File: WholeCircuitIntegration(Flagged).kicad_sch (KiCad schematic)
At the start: 18 parts, among them J1 Conn_02x20_Odd_Even, J2 Conn_01x03_Socket, J3 Conn_01x03_Socket, J4 Conn_01x03_Socket, J5 Conn_01x03_Socket, J6 TBP03R2-350-03BE, J7 TBP03R2-350-03BE, J8 TBP03R2-350-03BE, J9 TBP03R2-350-03BE, U1 ADS1115IDGS, U2 BNO055, U3 74LV14

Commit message: Whole Circuit Integration
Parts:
- removed C1: 120, Capacitor_SMD:CP_Elec_4x3, symbol Device:C
- removed C2, C4: 100 n, Capacitor_SMD:CP_Elec_4x3, symbol Device:C
- removed C3: 6.8 n, Capacitor_SMD:CP_Elec_4x3, symbol Device:C
- removed J1: Conn_02x20_Odd_Even, symbol Connector_Generic:Conn_02x20_Odd_Even
- removed J2, J3, J4, J5: Conn_01x03_Socket, symbol Connector:Conn_01x03_Socket
- removed J6, J7, J8, J9: TBP03R2-350-03BE, TBP03R2_350_03BE:CUI_TBP03R2-350-03BE, symbol TBP03R2-350-03BE:TBP03R2-350-03BE
- removed Optional1, Pull-Up1: 10k, Resistor_SMD:R_0603_1608Metric_Pad0.98x0.95mm_HandSolder, symbol Device:R
- removed U1: ADS1115IDGS, Package_SO:TSSOP-10_3x3mm_P0.5mm, symbol Analog_ADC:ADS1115IDGS
- removed U2: BNO055, Package_LGA:LGA-28_5.2x3.8mm_P0.5mm, symbol Sensor_Motion:BNO055
- removed U3: 74LV14, Package_DIP:DIP-12_W7.62mm, symbol 74xx:74LV14
- added J6: Conn_02x20_Odd_Even, symbol Connector_Generic:Conn_02x20_Odd_Even
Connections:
- net 3.3V: now also J6.1 (Pin_1), J6.17 (Pin_17)
- net 5,0_VDC: now also J6.2 (Pin_2)
- net 5V: now also J6.4 (Pin_4)
- net ADC ALERT (GPIO 04): now also J6.7 (Pin_7)
- net COM 3 (GPIO 19): now also J6.35 (Pin_35)
- net GND: now also J6.14 (Pin_14), J6.20 (Pin_20), J6.25 (Pin_25), J6.30 (Pin_30), J6.34 (Pin_34), J6.39 (Pin_39), J6.6 (Pin_6), J6.9 (Pin_9)
- net I2C_1_SCL: now also J6.28 (Pin_28)
- net I2C_1_SDA: now also J6.27 (Pin_27)
- net I2C_2_SCL: now also J6.5 (Pin_5)
- net I2C_2_SDA: now also J6.3 (Pin_3)
- net I2S_4_SCLK: now also J6.12 (Pin_12)
- net IMU nBOOT (GPIO 13): now also J6.33 (Pin_33)
- net IMU nRESET (GPIO 05): now also J6.29 (Pin_29)
- net LCD_TE: now also J6.15 (Pin_15)
- net SPI_1_CS0: now also J6.24 (Pin_24)
- net SPI_1_CS1: now also J6.26 (Pin_26)
- net SPI_1_MISO: now also J6.21 (Pin_21)
- net SPI_1_MOSI: now also J6.19 (Pin_19)
- net SPI_1_SCK: now also J6.23 (Pin_23)
- net SPI_2_CS0: now also J6.18 (Pin_18)
- net SPI_2_CS1: now also J6.16 (Pin_16)
- net SPI_2_MISO: now also J6.22 (Pin_22)
- net SPI_2_MOSI: now also J6.37 (Pin_37)
- net SPI_2_SCK: now also J6.13 (Pin_13)
- net ST 1 (GPIO 12): now also J6.32 (Pin_32)
- net ST 2 (GPIO 16): now also J6.36 (Pin_36), J6.38 (Pin_38)
- net ST 4 (GPIO 21): now also J6.40 (Pin_40)
- net UART_2_RTS: now also J6.11 (Pin_11)
- net UART_2_RX: now also J6.10 (Pin_10)
- net UART_2_TX: now also J6.8 (Pin_8)
- new net IMU INT (GPIO 16): J6.31 (Pin_31)
- no-connect marks 17 -> 9
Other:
- added sheet ADC (ADC.kicad_sch)
- added sheet IMU(BN0055) (IMU(BN0055).kicad_sch)
- added sheet SchmittTrigger(74LV14) (SchmittTrigger(74LV14).kicad_sch)
- note removed: "1 - V 2 - Signal 3 - GND"

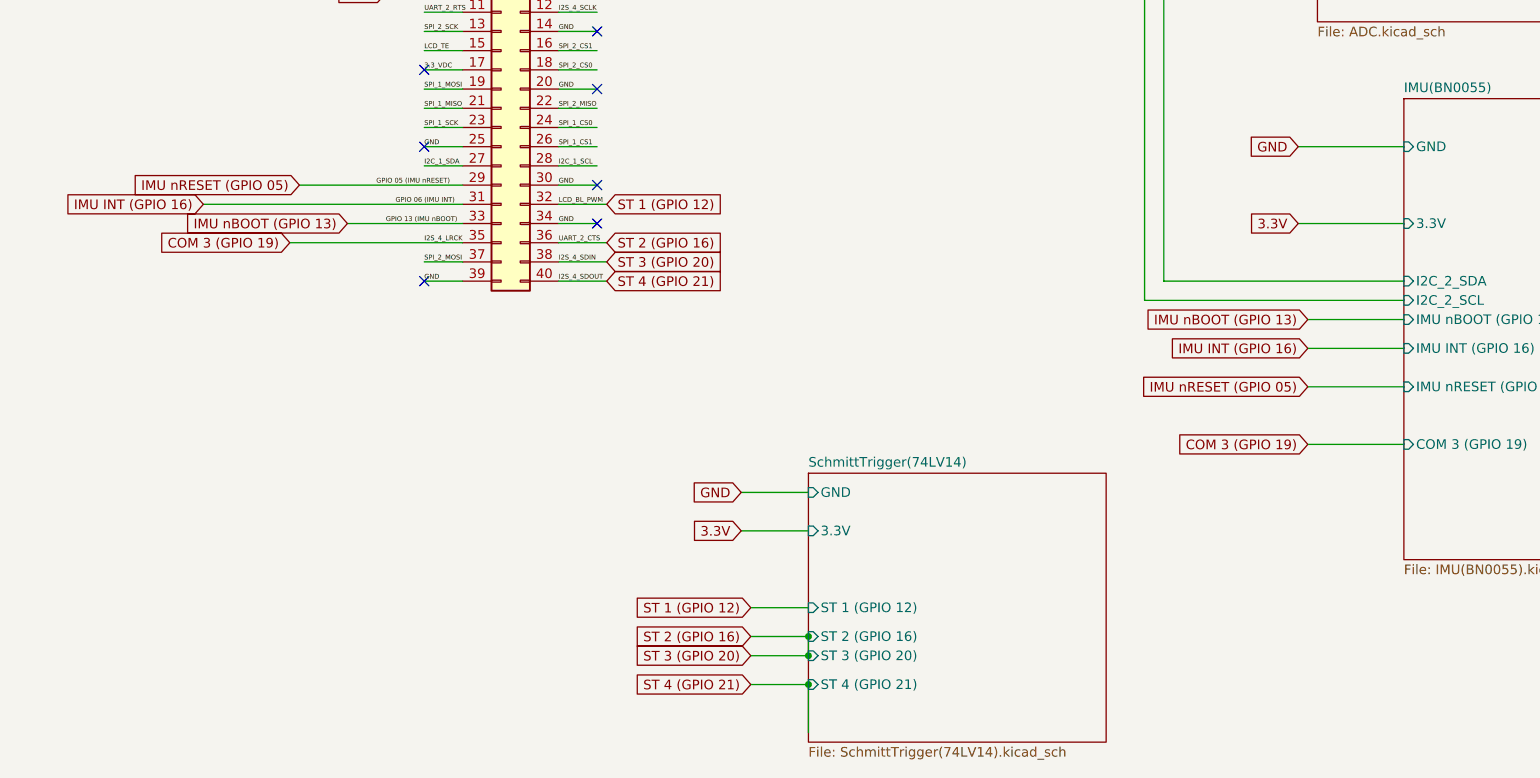
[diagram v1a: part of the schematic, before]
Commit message: Replaced sockets with terminal blocks
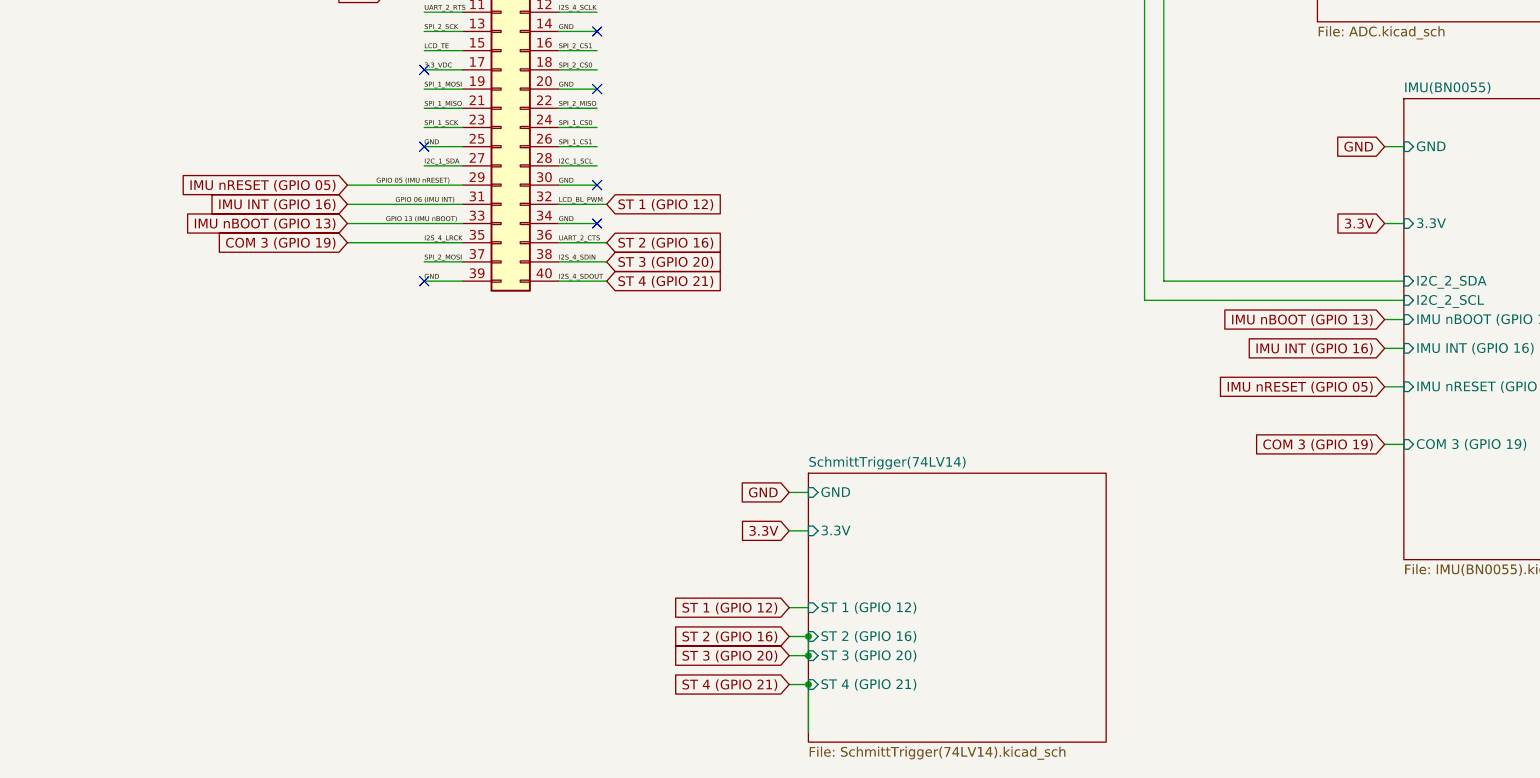
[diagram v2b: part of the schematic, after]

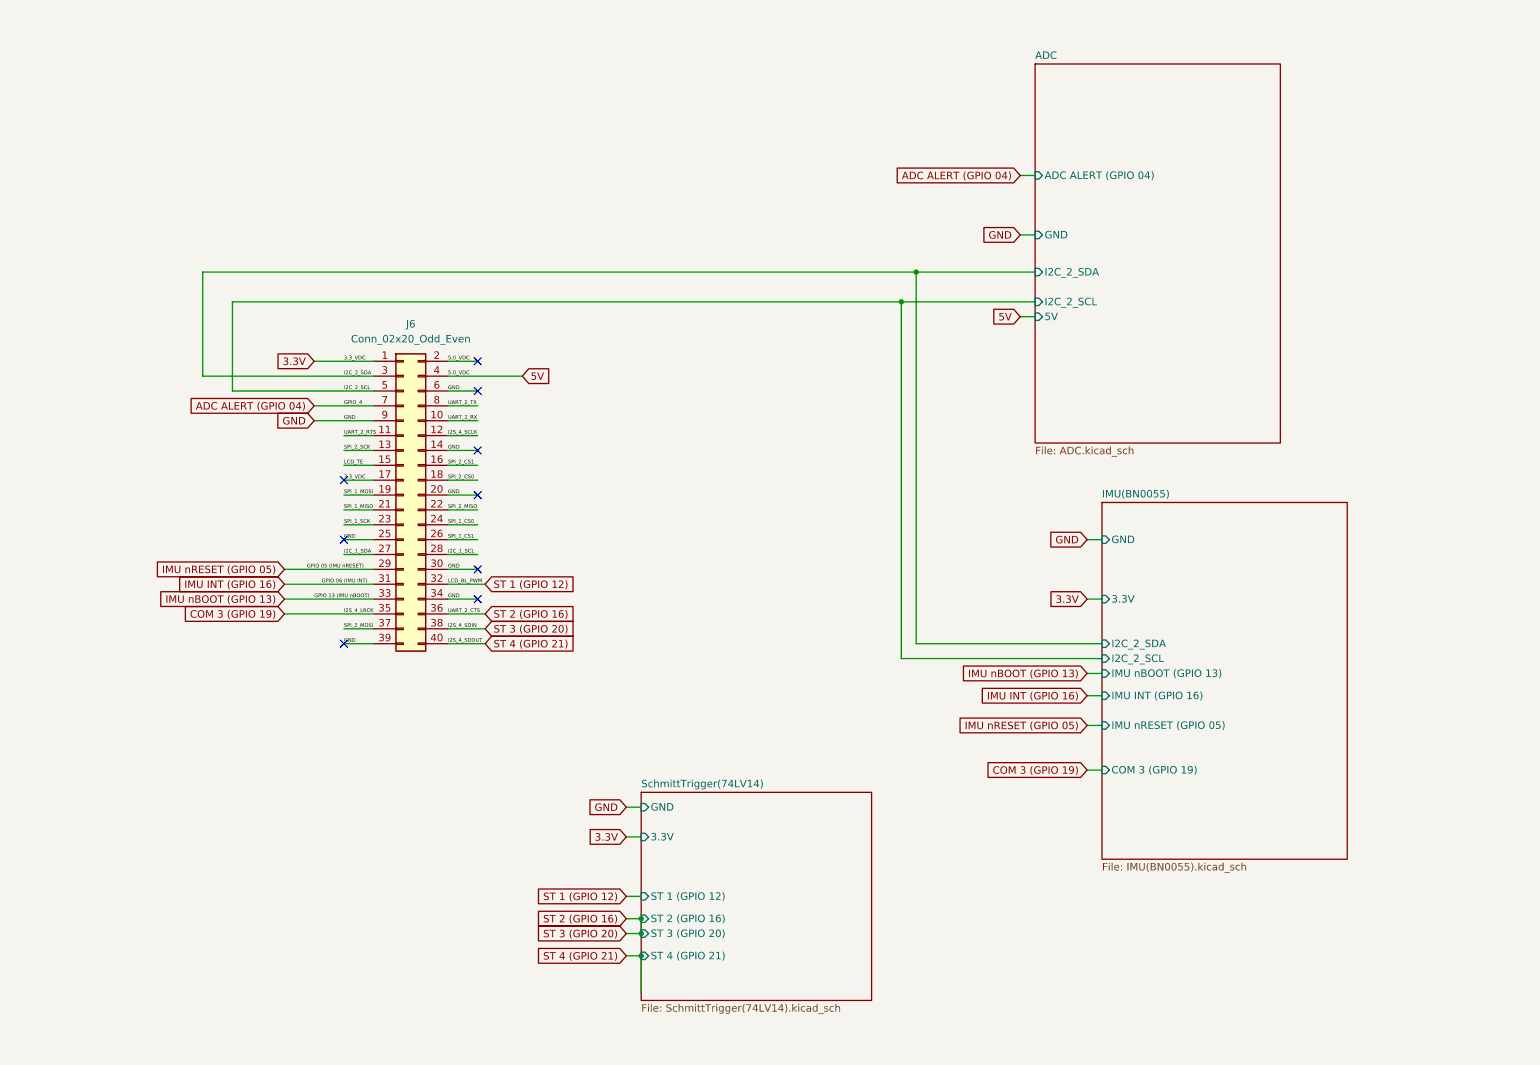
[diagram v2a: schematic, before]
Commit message: Reorganized schematic and resolved ERC errors
Resolved some of the ERC errors related to disconnected pins and power flags. Renamed GPIO pins on 40-pin header. Changed ADC power supply to 3.3V and schmitt trigger circuit power supply to 5V. Connected 5V, 3.3V, and GND pins of 40-pin header. Assigned footprint for 40-pin header based on dimensions of expansion header on Jetson Nano Carrier Board.

Also moved IMU and 40-pin header KiCAD project files into their own folders.
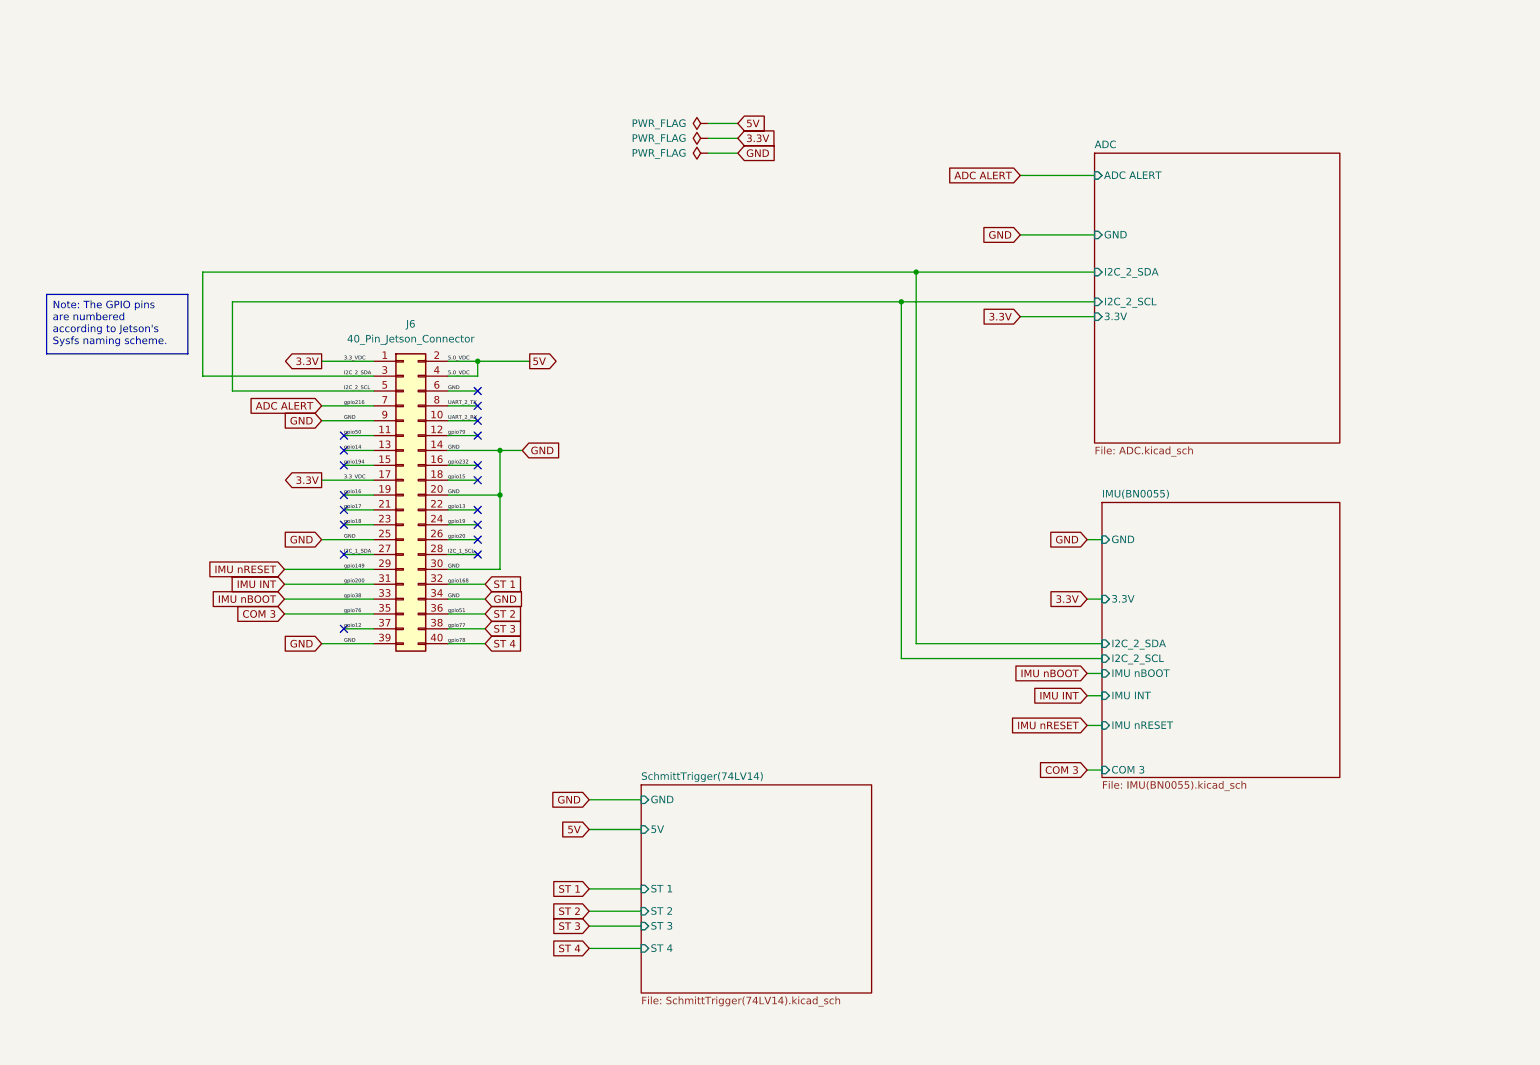
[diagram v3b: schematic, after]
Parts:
- J6: value Conn_02x20_Odd_Even -> 40_Pin_Jetson_Connector; footprint (none) -> Connector_PinHeader_2.54mm:PinHeader_2x20_P2.54mm_Vertical
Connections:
- net 5,0_VDC is gone; now on net 5V: J6.2 (Pin_2)
- net ADC ALERT (GPIO 04) renamed ADC ALERT
- net COM 3 (GPIO 19) renamed COM 3
- net I2S_4_SCLK renamed gpio79
- net IMU INT (GPIO 16) renamed IMU INT
- net IMU nBOOT (GPIO 13) renamed IMU nBOOT
- net IMU nRESET (GPIO 05) renamed IMU nRESET
- net LCD_TE renamed gpio194
- net SPI_1_CS0 renamed gpio19
- net SPI_1_CS1 renamed gpio20
- net SPI_1_MISO renamed gpio17
- net SPI_1_MOSI renamed gpio16
- net SPI_1_SCK renamed gpio18
- net SPI_2_CS0 renamed gpio15
- net SPI_2_CS1 renamed gpio232
- net SPI_2_MISO renamed gpio13
- net SPI_2_MOSI renamed gpio12
- net SPI_2_SCK renamed gpio14
- net ST 1 (GPIO 12) renamed ST 1
- net ST 2 (GPIO 16) renamed ST 2
- net ST 2: no longer J6.38 (Pin_38)
- net ST 4 (GPIO 21) renamed ST 4
- net UART_2_RTS renamed gpio50
- new net ST 3: J6.38 (Pin_38)
- no-connect marks 9 -> 18
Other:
- sheet ADC ports: added 3.3V, ADC ALERT; removed 5V, ADC ALERT (GPIO 04)
- sheet IMU(BN0055) ports: added COM 3, IMU INT, IMU nBOOT, IMU nRESET; removed COM 3 (GPIO 19), IMU INT (GPIO 16), IMU nBOOT (GPIO 13), IMU nRESET (GPIO 05)
- sheet SchmittTrigger(74LV14) ports: added 5V, ST 1, ST 2, ST 3, ST 4; removed 3.3V, ST 1 (GPIO 12), ST 2 (GPIO 16), ST 3 (GPIO 20), ST 4 (GPIO 21)
